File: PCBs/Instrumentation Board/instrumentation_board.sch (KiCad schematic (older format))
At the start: 17 parts, among them J1 Conn_01x02, J2 Conn_01x02, Q1 Q_Photo_NPN, U1 GPS-ADAFRUIT746, U2 LSM6DS3HTR, U3 LSM6DS3HTR, U4 MS5607-02BA03, U5 MicroSD-ADAFRUIT254

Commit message: Fixed weird merge issue (2)
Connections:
- net Sheet5ABF9899/THERM_OUT is gone; now on net Sheet5ABF9899/THERM_OUT: A1.21 (AD2/D16)
- net Sheet5ABF9899/THERM_OUT: no longer A1.20 (AD1/D15)
- net Sheet5ABF9899/THERM_OUT renamed Sheet5ABF9899_3/THERM_OUT
- new net Sheet5ABF9899_2/THERM_OUT: A1.20 (AD1/D15)
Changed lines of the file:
@@
 S 3450 5450 650  300
 U 5ABF989A
-F0 "Sheet5ABF9899" 60
+F0 "Sheet5ABF9899_2" 60
 F1 "file5ABF9899.sch" 60
 F2 "THERM_OUT" I L 3450 5600 60
@@
 S 3450 6450 650  300
 U 5ABFB538
-F0 "Sheet5ABF9899" 60
+F0 "Sheet5ABF9899_3" 60
 F1 "file5ABF9899.sch" 60
 F2 "THERM_OUT" I L 3450 6600 60

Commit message: review changes + instr board PCB
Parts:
- added R10, R7, R8, R9: 0, Resistors_SMD:R_0805_HandSoldering, symbol R
- C1, C2, C3, C4, C5: footprint (none) -> Capacitors_SMD:C_0805_HandSoldering
- Q1: value Q_Photo_NPN -> TEMT6000X01; footprint (none) -> Diodes_SMD:D_1206
- R1, R2, R3: footprint (none) -> Resistors_SMD:R_0805_HandSoldering
- U2: footprint Instrumentation Footprints:LGA-14 -> lga:LGA-14
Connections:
- net GPS_IN: now also R7.1, R9.1; no longer A1.1 (D0/TX)
- net GPS_OUT: now also R10.1, R8.1; no longer A1.2 (D1/RX)
- net at A1.7 (D4): now also R9.2
- net at A1.8 (D5): now also R10.2
- new net: A1.1 (D0/TX), R7.2
- new net: A1.2 (D1/RX), R8.2
- no-connect marks 23 -> 21
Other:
- moved on the sheet: R2
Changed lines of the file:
@@
 $EndComp
 $Comp
-L GND #PWR3
+L GND #PWR01
 U 1 1 5A9B0C4F
 P 2350 2000
-F 0 "#PWR3" H 2350 1750 50  0001 C CNN
+F 0 "#PWR01" H 2350 1750 50  0001 C CNN
 F 1 "GND" H 2350 1850 50  0000 C CNN
 F 2 "" H 2350 2000 50  0001 C CNN
@@
 7.4V
 $Comp
-L GND #PWR2
+L GND #PWR02
 U 1 1 5A9B0CC8
 P 1400 6600
-F 0 "#PWR2" H 1400 6350 50  0001 C CNN
+F 0 "#PWR02" H 1400 6350 50  0001 C CNN
 F 1 "GND" H 1400 6450 50  0000 C CNN
 F 2 "" H 1400 6600 50  0001 C CNN
@@
 $EndComp
 $Comp
-L GND #PWR1
+L GND #PWR03
 U 1 1 5A9B0CDD
 P 1250 6600
-F 0 "#PWR1" H 1250 6350 50  0001 C CNN
+F 0 "#PWR03" H 1250 6350 50  0001 C CNN
 F 1 "GND" H 1250 6450 50  0000 C CNN
 F 2 "" H 1250 6600 50  0001 C CNN
@@
 $EndComp
 $Comp
-L GND #PWR5
+L GND #PWR04
 U 1 1 5A9B5B00
 P 6700 6100
-F 0 "#PWR5" H 6700 5850 50  0001 C CNN
+F 0 "#PWR04" H 6700 5850 50  0001 C CNN
 F 1 "GND" H 6700 5950 50  0000 C CNN
 F 2 "" H 6700 6100 50  0001 C CNN
@@
 	1    0    0    -1
 $EndComp
-Text GLabel 2800 4500 2    60   Input ~ 0
+Text GLabel 3550 4500 2    60   Input ~ 0
 GPS_IN
-Text GLabel 2800 4600 2    60   Input ~ 0
+Text GLabel 3550 4600 2    60   Input ~ 0
 GPS_OUT
 Text GLabel 7150 6050 0    60   Input ~ 0
@@
 F 0 "C3" H 7425 4300 50  0000 L CNN
 F 1 "100nF" H 7425 4100 50  0000 L CNN
-F 2 "" H 7438 4050 50  0001 C CNN
+F 2 "Capacitors_SMD:C_0805_HandSoldering" H 7438 4050 50  0001 C CNN
 F 3 "" H 7400 4200 50  0001 C CNN
 	1    7400 4200
@@
 $EndComp
 $Comp
-L GND #PWR8
+L GND #PWR05
 U 1 1 5AA0BCD5
 P 7400 4350
-F 0 "#PWR8" H 7400 4100 50  0001 C CNN
+F 0 "#PWR05" H 7400 4100 50  0001 C CNN
 F 1 "GND" H 7400 4200 50  0000 C CNN
 F 2 "" H 7400 4350 50  0001 C CNN
@@
 $EndComp
 $Comp
-L GND #PWR10
+L GND #PWR06
 U 1 1 5AA0BE17
 P 7700 4350
-F 0 "#PWR10" H 7700 4100 50  0001 C CNN
+F 0 "#PWR06" H 7700 4100 50  0001 C CNN
 F 1 "GND" H 7700 4200 50  0000 C CNN
 F 2 "" H 7700 4350 50  0001 C CNN
@@
 SS
 $Comp
-L GND #PWR13
+L GND #PWR07
 U 1 1 5AA0CF85
 P 7800 5050
-F 0 "#PWR13" H 7800 4800 50  0001 C CNN
+F 0 "#PWR07" H 7800 4800 50  0001 C CNN
 F 1 "GND" H 7800 4900 50  0000 C CNN
 F 2 "" H 7800 5050 50  0001 C CNN
@@
 F 0 "U2" H 8400 1650 60  0000 C CNN
 F 1 "LSM6DS3HTR" H 8400 850 60  0000 C CNN
-F 2 "Instrumentation Footprints:LGA-14" H 8450 1300 60  0001 C CNN
+F 2 "lga:LGA-14" H 8450 1300 60  0001 C CNN
 F 3 "" H 8450 1300 60  0001 C CNN
 	1    8400 1300
@@
 $EndComp
 $Comp
-L GND #PWR14
+L GND #PWR08
 U 1 1 5AA21112
 P 9900 1550
-F 0 "#PWR14" H 9900 1300 50  0001 C CNN
+F 0 "#PWR08" H 9900 1300 50  0001 C CNN
 F 1 "GND" H 9900 1400 50  0000 C CNN
 F 2 "" H 9900 1550 50  0001 C CNN
@@
 F 0 "C4" H 9925 1500 50  0000 L CNN
 F 1 "100nF" H 9925 1300 50  0000 L CNN
-F 2 "" H 9938 1250 50  0001 C CNN
+F 2 "Capacitors_SMD:C_0805_HandSoldering" H 9938 1250 50  0001 C CNN
 F 3 "" H 9900 1400 50  0001 C CNN
 	1    9900 1400
@@
 F 0 "C1" H 7175 1700 50  0000 L CNN
 F 1 "100nF" H 7175 1500 50  0000 L CNN
-F 2 "" H 7188 1450 50  0001 C CNN
+F 2 "Capacitors_SMD:C_0805_HandSoldering" H 7188 1450 50  0001 C CNN
 F 3 "" H 7150 1600 50  0001 C CNN
 	1    7150 1600
@@
 $EndComp
 $Comp
-L GND #PWR6
+L GND #PWR09
 U 1 1 5AA21334
 P 7150 1750
-F 0 "#PWR6" H 7150 1500 50  0001 C CNN
+F 0 "#PWR09" H 7150 1500 50  0001 C CNN
 F 1 "GND" H 7150 1600 50  0000 C CNN
 F 2 "" H 7150 1750 50  0001 C CNN
@@
 $EndComp
 $Comp
-L GND #PWR11
+L GND #PWR010
 U 1 1 5AA735F3
 P 7750 1850
-F 0 "#PWR11" H 7750 1600 50  0001 C CNN
+F 0 "#PWR010" H 7750 1600 50  0001 C CNN
 F 1 "GND" H 7750 1700 50  0000 C CNN
 F 2 "" H 7750 1850 50  0001 C CNN
@@
 $EndComp
 $Comp
-L GND #PWR15
+L GND #PWR011
 U 1 1 5AA87752
 P 9900 2900
-F 0 "#PWR15" H 9900 2650 50  0001 C CNN
+F 0 "#PWR011" H 9900 2650 50  0001 C CNN
 F 1 "GND" H 9900 2750 50  0000 C CNN
 F 2 "" H 9900 2900 50  0001 C CNN
@@
 F 0 "C5" H 9925 2850 50  0000 L CNN
 F 1 "100nF" H 9925 2650 50  0000 L CNN
-F 2 "" H 9938 2600 50  0001 C CNN
+F 2 "Capacitors_SMD:C_0805_HandSoldering" H 9938 2600 50  0001 C CNN
 F 3 "" H 9900 2750 50  0001 C CNN
 	1    9900 2750
@@
 F 0 "C2" H 7175 3050 50  0000 L CNN
 F 1 "100nF" H 7175 2850 50  0000 L CNN
-F 2 "" H 7188 2800 50  0001 C CNN
+F 2 "Capacitors_SMD:C_0805_HandSoldering" H 7188 2800 50  0001 C CNN
 F 3 "" H 7150 2950 50  0001 C CNN
 	1    7150 2950
@@
 $EndComp
 $Comp
-L GND #PWR7
+L GND #PWR012
 U 1 1 5AA87764
 P 7150 3100
-F 0 "#PWR7" H 7150 2850 50  0001 C CNN
+F 0 "#PWR012" H 7150 2850 50  0001 C CNN
 F 1 "GND" H 7150 2950 50  0000 C CNN
 F 2 "" H 7150 3100 50  0001 C CNN
@@
 $EndComp
 $Comp
-L GND #PWR12
+L GND #PWR013
 U 1 1 5AA8776A
 P 7750 3200
-F 0 "#PWR12" H 7750 2950 50  0001 C CNN
+F 0 "#PWR013" H 7750 2950 50  0001 C CNN
 F 1 "GND" H 7750 3050 50  0000 C CNN
 F 2 "" H 7750 3200 50  0001 C CNN
@@
 INT1_1.8V
 $Comp
-L GND #PWR9
+L GND #PWR014
 U 1 1 5AA87956
 P 7600 950
-F 0 "#PWR9" H 7600 700 50  0001 C CNN
+F 0 "#PWR014" H 7600 700 50  0001 C CNN
 F 1 "GND" H 7600 800 50  0000 C CNN
 F 2 "" H 7600 950 50  0001 C CNN
@@
 NoConn ~ 2800 5200
 NoConn ~ 2800 5100
-NoConn ~ 2800 5000
-NoConn ~ 2800 4900
 NoConn ~ 1450 5700
 NoConn ~ 1450 5250
@@
 1.8V
 $Comp
-L GND #PWR4
+L GND #PWR015
 U 1 1 5AB3D6CF
 P 5050 2400
-F 0 "#PWR4" H 5050 2150 50  0001 C CNN
+F 0 "#PWR015" H 5050 2150 50  0001 C CNN
 F 1 "GND" H 5050 2250 50  0000 C CNN
 F 2 "" H 5050 2400 50  0001 C CNN
@@
 F 0 "R3" V 5130 2250 50  0000 C CNN
 F 1 "10K" V 5050 2250 50  0000 C CNN
-F 2 "" V 4980 2250 50  0001 C CNN
+F 2 "Resistors_SMD:R_0805_HandSoldering" V 4980 2250 50  0001 C CNN
 F 3 "" H 5050 2250 50  0001 C CNN
 	1    5050 2250
@@
 P 5400 2000
 F 0 "Q1" H 5600 2050 50  0000 L CNN
-F 1 "Q_Photo_NPN" H 5600 1950 50  0000 L CNN
-F 2 "" H 5600 2100 50  0001 C CNN
+F 1 "TEMT6000X01" H 5600 1950 50  0000 L CNN
+F 2 "Diodes_SMD:D_1206" H 5600 2100 50  0001 C CNN
 F 3 "" H 5400 2000 50  0001 C CNN
 	1    5400 2000
@@
 Text GLabel 3100 4700 2    60   Input ~ 0
 INT1_5V
-Text GLabel 3400 4800 2    60   Input ~ 0
+Text GLabel 3100 4800 2    60   Input ~ 0
 INT0_5V
 $Comp
@@
 U 1 1 5AB8F25C
 P 2950 4700
-F 0 "R1" V 3030 4700 50  0000 C CNN
+F 0 "R1" V 3000 4550 50  0000 C CNN
 F 1 "0" V 2950 4700 50  0000 C CNN
-F 2 "" V 2880 4700 50  0001 C CNN
+F 2 "Resistors_SMD:R_0805_HandSoldering" V 2880 4700 50  0001 C CNN
 F 3 "" H 2950 4700 50  0001 C CNN
 	1    2950 4700
@@
 L R R2
 U 1 1 5AB8F757
-P 3250 4800
-F 0 "R2" V 3330 4800 50  0000 C CNN
-F 1 "0" V 3250 4800 50  0000 C CNN
-F 2 "" V 3180 4800 50  0001 C CNN
-F 3 "" H 3250 4800 50  0001 C CNN
-	1    3250 4800
+P 2950 4800
+F 0 "R2" V 3000 4650 50  0000 C CNN
+F 1 "0" V 2950 4800 50  0000 C CNN
+F 2 "Resistors_SMD:R_0805_HandSoldering" V 2880 4800 50  0001 C CNN
+F 3 "" H 2950 4800 50  0001 C CNN
+	1    2950 4800
 	0    1    1    0
 $EndComp
@@
 Connection ~ 5400 3500
 Wire Wire Line
-	2800 4800 3100 4800
+	2800 4800 2800 4800
 Wire Wire Line
 	8600 5850 8950 5850
@@
 Wire Wire Line
 	2800 6100 3450 6100
+Text GLabel 3550 4900 2    60   Input ~ 0
+GPS_IN
+Text GLabel 3550 5000 2    60   Input ~ 0
+GPS_OUT
+$Comp
+L R R8
+U 1 1 5AC0BBA1
+P 2950 4600
+F 0 "R8" V 3000 4450 50  0000 C CNN
+F 1 "0" V 2950 4600 50  0000 C CNN
+F 2 "Resistors_SMD:R_0805_HandSoldering" V 2880 4600 50  0001 C CNN
+F 3 "" H 2950 4600 50  0001 C CNN
+	1    2950 4600
+	0    1    1    0
+$EndComp
+$Comp
+L R R7
+U 1 1 5AC0BCB9
+P 2950 4500
+F 0 "R7" V 3000 4350 50  0000 C CNN
+F 1 "0" V 2950 4500 50  0000 C CNN
+F 2 "Resistors_SMD:R_0805_HandSoldering" V 2880 4500 50  0001 C CNN
+F 3 "" H 2950 4500 50  0001 C CNN
+	1    2950 4500
+	0    1    1    0
+$EndComp
+$Comp
+L R R9
+U 1 1 5AC0BDD4
+P 2950 4900
+F 0 "R9" V 3000 4750 50  0000 C CNN
+F 1 "0" V 2950 4900 50  0000 C CNN
+F 2 "Resistors_SMD:R_0805_HandSoldering" V 2880 4900 50  0001 C CNN
+F 3 "" H 2950 4900 50  0001 C CNN
+	1    2950 4900
+	0    1    1    0
+$EndComp
+$Comp
+L R R10
+U 1 1 5AC0BEF2
+P 2950 5000
+F 0 "R10" V 3000 4850 50  0000 C CNN
+F 1 "0" V 2950 5000 50  0000 C CNN
+F 2 "Resistors_SMD:R_0805_HandSoldering" V 2880 5000 50  0001 C CNN
+F 3 "" H 2950 5000 50  0001 C CNN
+	1    2950 5000
+	0    1    1    0
+$EndComp
+Wire Wire Line
+	3550 4500 3100 4500
+Wire Wire Line
+	3100 4600 3550 4600
+Wire Wire Line
+	3100 4900 3550 4900
+Wire Wire Line
+	3100 5000 3550 5000
 $EndSCHEMATC

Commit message: finished traces on instr board
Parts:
- removed C4, C5: 100nF, Capacitors_SMD:C_0805_HandSoldering, symbol C
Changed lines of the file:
@@
-$EndComp
-$Comp
-L GND #PWR08
-U 1 1 5AA21112
-P 9900 1550
-F 0 "#PWR08" H 9900 1300 50  0001 C CNN
-F 1 "GND" H 9900 1400 50  0000 C CNN
-F 2 "" H 9900 1550 50  0001 C CNN
-F 3 "" H 9900 1550 50  0001 C CNN
-	1    9900 1550
-	1    0    0    -1
-$EndComp
-$Comp
-L C C4
-U 1 1 5AA2114D
-P 9900 1400
-F 0 "C4" H 9925 1500 50  0000 L CNN
-F 1 "100nF" H 9925 1300 50  0000 L CNN
-F 2 "Capacitors_SMD:C_0805_HandSoldering" H 9938 1250 50  0001 C CNN
-F 3 "" H 9900 1400 50  0001 C CNN
-	1    9900 1400
-	1    0    0    -1
 $EndComp
 $Comp
@@
 F 3 "" H 8450 2650 60  0001 C CNN
 	1    8400 2650
-	1    0    0    -1
-$EndComp
-$Comp
-L GND #PWR011
-U 1 1 5AA87752
-P 9900 2900
-F 0 "#PWR011" H 9900 2650 50  0001 C CNN
-F 1 "GND" H 9900 2750 50  0000 C CNN
-F 2 "" H 9900 2900 50  0001 C CNN
-F 3 "" H 9900 2900 50  0001 C CNN
-	1    9900 2900
-	1    0    0    -1
-$EndComp
-$Comp
-L C C5
-U 1 1 5AA87758
-P 9900 2750
-F 0 "C5" H 9925 2850 50  0000 L CNN
-F 1 "100nF" H 9925 2650 50  0000 L CNN
-F 2 "Capacitors_SMD:C_0805_HandSoldering" H 9938 2600 50  0001 C CNN
-F 3 "" H 9900 2750 50  0001 C CNN
-	1    9900 2750
 	1    0    0    -1
 $EndComp
@@
 Wire Wire Line
 	9550 2800 9000 2800
-Connection ~ 9550 2400
-Wire Wire Line
-	9900 2400 9900 2600
 Connection ~ 7150 2400
 Wire Wire Line
 	7150 2800 7750 2800
-Wire Wire Line
-	9000 2400 9900 2400
 Wire Wire Line
 	9550 2150 9550 2800
@@
 Wire Wire Line
 	9550 1450 9000 1450
-Connection ~ 9550 1050
-Wire Wire Line
-	9900 1050 9900 1250
 Wire Wire Line
 	7150 1450 7750 1450
-Wire Wire Line
-	9000 1050 9900 1050
 Wire Wire Line
 	9550 800  9550 1450
@@
 Wire Wire Line
 	3100 5000 3550 5000
+Wire Wire Line
+	9000 2400 9550 2400
+Connection ~ 9550 2400
+Wire Wire Line
+	9000 1050 9550 1050
+Connection ~ 9550 1050
 $EndSCHEMATC

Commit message: rerouted payload instr board and completed all changes per Alexs review
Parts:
- U2, U3: footprint lga:LGA-14 -> LGA_Long:LGA-14
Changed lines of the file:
@@
 F 0 "U2" H 8400 1650 60  0000 C CNN
 F 1 "LSM6DS3HTR" H 8400 850 60  0000 C CNN
-F 2 "lga:LGA-14" H 8450 1300 60  0001 C CNN
+F 2 "LGA_Long:LGA-14" H 8450 1300 60  0001 C CNN
 F 3 "" H 8450 1300 60  0001 C CNN
 	1    8400 1300
@@
 $EndComp
 $Comp
-L GND #PWR09
+L GND #PWR08
 U 1 1 5AA21334
 P 7150 1750
-F 0 "#PWR09" H 7150 1500 50  0001 C CNN
+F 0 "#PWR08" H 7150 1500 50  0001 C CNN
 F 1 "GND" H 7150 1600 50  0000 C CNN
 F 2 "" H 7150 1750 50  0001 C CNN
@@
 $EndComp
 $Comp
-L GND #PWR010
+L GND #PWR09
 U 1 1 5AA735F3
 P 7750 1850
-F 0 "#PWR010" H 7750 1600 50  0001 C CNN
+F 0 "#PWR09" H 7750 1600 50  0001 C CNN
 F 1 "GND" H 7750 1700 50  0000 C CNN
 F 2 "" H 7750 1850 50  0001 C CNN
@@
 F 0 "U3" H 8400 3000 60  0000 C CNN
 F 1 "LSM6DS3HTR" H 8400 2200 60  0000 C CNN
-F 2 "lga:LGA-14" H 8450 2650 60  0001 C CNN
+F 2 "LGA_Long:LGA-14" H 8450 2650 60  0001 C CNN
 F 3 "" H 8450 2650 60  0001 C CNN
 	1    8400 2650
@@
 $EndComp
 $Comp
-L GND #PWR012
+L GND #PWR010
 U 1 1 5AA87764
 P 7150 3100
-F 0 "#PWR012" H 7150 2850 50  0001 C CNN
+F 0 "#PWR010" H 7150 2850 50  0001 C CNN
 F 1 "GND" H 7150 2950 50  0000 C CNN
 F 2 "" H 7150 3100 50  0001 C CNN
@@
 $EndComp
 $Comp
-L GND #PWR013
+L GND #PWR011
 U 1 1 5AA8776A
 P 7750 3200
-F 0 "#PWR013" H 7750 2950 50  0001 C CNN
+F 0 "#PWR011" H 7750 2950 50  0001 C CNN
 F 1 "GND" H 7750 3050 50  0000 C CNN
 F 2 "" H 7750 3200 50  0001 C CNN
@@
 INT1_1.8V
 $Comp
-L GND #PWR014
+L GND #PWR012
 U 1 1 5AA87956
 P 7600 950
-F 0 "#PWR014" H 7600 700 50  0001 C CNN
+F 0 "#PWR012" H 7600 700 50  0001 C CNN
 F 1 "GND" H 7600 800 50  0000 C CNN
 F 2 "" H 7600 950 50  0001 C CNN
@@
 1.8V
 $Comp
-L GND #PWR015
+L GND #PWR013
 U 1 1 5AB3D6CF
 P 5050 2400
-F 0 "#PWR015" H 5050 2150 50  0001 C CNN
+F 0 "#PWR013" H 5050 2150 50  0001 C CNN
 F 1 "GND" H 5050 2250 50  0000 C CNN
 F 2 "" H 5050 2400 50  0001 C CNN

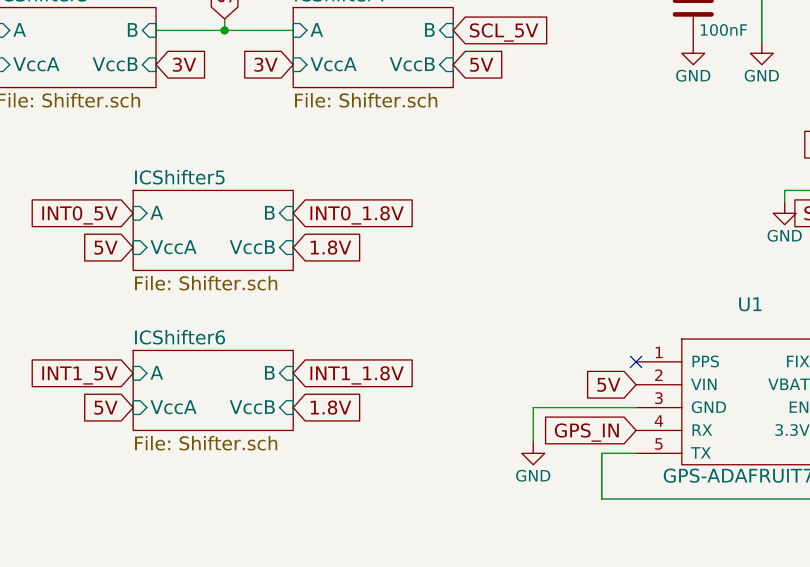
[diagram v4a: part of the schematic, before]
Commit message: Fixed instr and recovery components per Alexs review
Added IMU current limiting resistors
Moved the caps near J4 on instr
Swapped out phototransistor footprint
Flipped I2C silk screen on J1 recovery
Flipped GND and TX silk screen on J6 recovery
renamed strat to alt on recovery silk screen
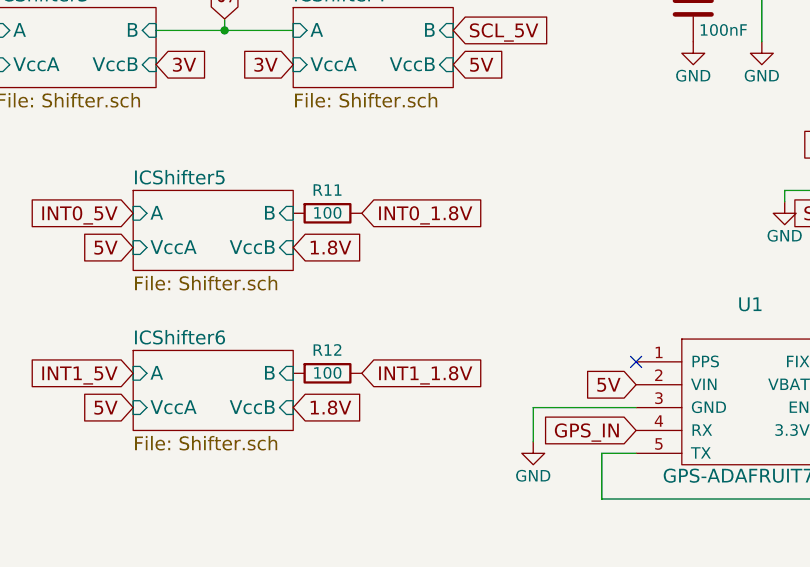
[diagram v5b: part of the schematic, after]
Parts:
- added R11, R12: 100, Resistors_SMD:R_0805_HandSoldering, symbol R
- Q1: footprint Diodes_SMD:D_1206 -> TEMT6000X01:TEMT6000X01
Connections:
- net INT0_1.8V: now also R11.1
- net INT1_1.8V: now also R12.1
- new net ICShifter5/B: R11.2
- new net ICShifter6/B: R12.2
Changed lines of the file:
@@
 F 0 "Q1" H 5600 2050 50  0000 L CNN
 F 1 "TEMT6000X01" H 5600 1950 50  0000 L CNN
-F 2 "Diodes_SMD:D_1206" H 5600 2100 50  0001 C CNN
+F 2 "TEMT6000X01:TEMT6000X01" H 5600 2100 50  0001 C CNN
 F 3 "" H 5400 2000 50  0001 C CNN
 	1    5400 2000
@@
 Text GLabel 4950 5250 0    60   Input ~ 0
 5V
-Text GLabel 5650 5100 2    60   Input ~ 0
+Text GLabel 5950 5100 2    60   Input ~ 0
 INT0_1.8V
 $Sheet
@@
 Text GLabel 4950 5800 0    60   Input ~ 0
 INT1_5V
-Text GLabel 5650 5800 2    60   Input ~ 0
+Text GLabel 5950 5800 2    60   Input ~ 0
 INT1_1.8V
 Text GLabel 3100 4700 2    60   Input ~ 0
@@
 	9000 1050 9550 1050
 Connection ~ 9550 1050
+$Comp
+L R R11
+U 1 1 5ACAE98D
+P 5800 5100
+F 0 "R11" V 5700 5100 50  0000 C CNN
+F 1 "100" V 5800 5100 50  0000 C CNN
+F 2 "Resistors_SMD:R_0805_HandSoldering" V 5730 5100 50  0001 C CNN
+F 3 "" H 5800 5100 50  0001 C CNN
+	1    5800 5100
+	0    1    1    0
+$EndComp
+$Comp
+L R R12
+U 1 1 5ACB0DCF
+P 5800 5800
+F 0 "R12" V 5700 5800 50  0000 C CNN
+F 1 "100" V 5800 5800 50  0000 C CNN
+F 2 "Resistors_SMD:R_0805_HandSoldering" V 5730 5800 50  0001 C CNN
+F 3 "" H 5800 5800 50  0001 C CNN
+	1    5800 5800
+	0    1    1    0
+$EndComp
 $EndSCHEMATC
